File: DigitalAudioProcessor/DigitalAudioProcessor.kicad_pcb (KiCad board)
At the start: 4 copper layers, 40 x 40 mm, 65 parts, among them J1 SWD, J2 I2S_OUT, J3 I2S_1, J4 USB, J5 I2S_3, J6 I2C, J7 I2S_2, J8 3.3V, U1 TOSLINK_RX, U2 USBLC6-2SC6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

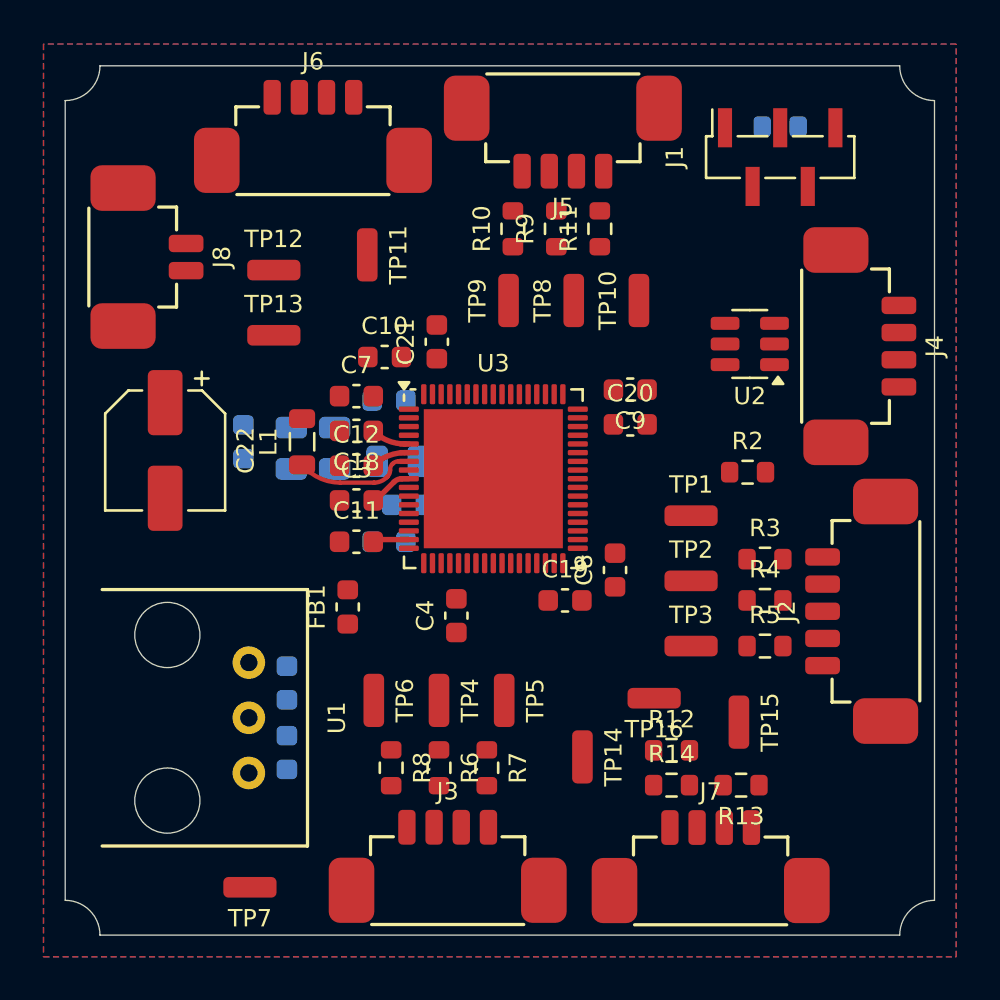
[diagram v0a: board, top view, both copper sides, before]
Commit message: DigitalAudioProcessor PCB done
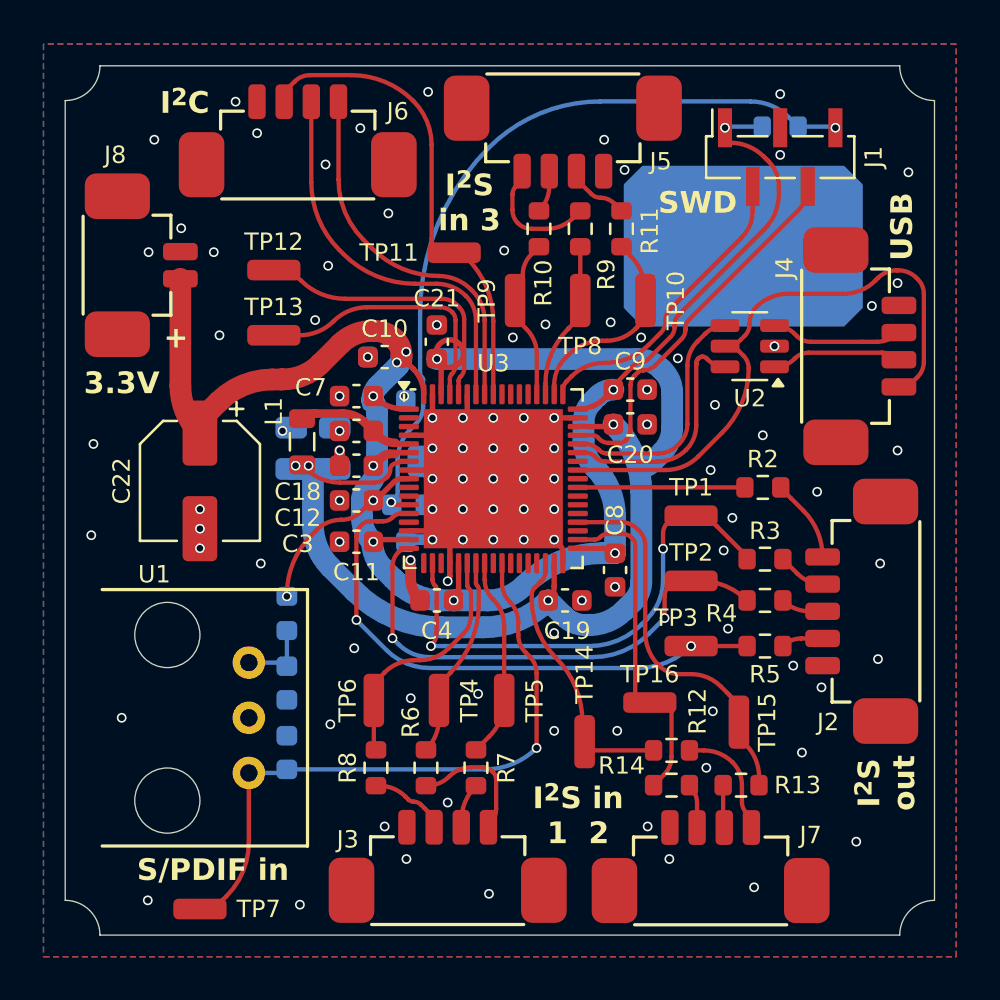
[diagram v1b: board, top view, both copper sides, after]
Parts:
- added REF**: BW_Logo_10x6.4mm, BW_Logo:BW_Logo_10x6.4mm, B.Cu at (161.2, 88.3)
- FB1: moved to B.Cu
- moved C2 7.58 mm to (144.7, 93.4), turned to 0 degrees
- moved TP11 4.00 mm to (147.9, 88.6), turned to 0 degrees
- moved FB1 2.82 mm to (140.2, 105.2), turned to -90 degrees
- moved TP7 2.51 mm to (136.2, 118.8)
- moved C22 2.13 mm to (136.2, 99.1)
- moved R10 1.20 mm to (151.8, 87.5)
- moved C4 1.14 mm to (147.1, 104.6), turned to 0 degrees
- moved R9 1.10 mm to (153.7, 87.5)
- moved R11 1.00 mm to (155.6, 87.5)
- moved R2 0.99 mm to (162.1, 99.4)
- moved J6 0.73 mm to (140.7, 84.1)
- moved TP14 0.71 mm to (153.9, 111.1)
- moved R8 0.70 mm to (144.3, 112.3)
- moved R6 0.60 mm to (146.6, 112.3)
- moved R7 0.50 mm to (148.9, 112.3)
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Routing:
- net +3.3V: track 5.46 -> 90.5 mm, vias 0 -> 11
- net VCC: track 5.66 -> 58.3 mm, vias 0 -> 5
- net Net-(J1-Pin_5): track 0.00 -> 35.4 mm, vias 0 -> 2
- net Net-(U1-OUT): track 0.00 -> 29.8 mm, vias 0 -> 1
- net Net-(J4-Pin_1): track 0.00 -> 28.3 mm
- net /I2S_OUT_LRCK: track 0.00 -> 25.8 mm, vias 0 -> 2
- net GND: track 0.00 -> 23.5 mm, vias 0 -> 106
- net Net-(U3-PA2): track 0.00 -> 23.4 mm, vias 0 -> 2
- net Net-(U3-PA0): track 0.00 -> 23.3 mm, vias 0 -> 2
- net Net-(J6-Pin_3): track 0.00 -> 22.1 mm
- net Net-(J6-Pin_2): track 0.00 -> 18.2 mm
- net /SWDIO: track 0.00 -> 17.5 mm
- net Net-(U3-PB14): track 0.00 -> 17.5 mm
- net Net-(J6-Pin_1): track 0.00 -> 17.2 mm
- net Net-(U3-PB12): track 0.00 -> 15.6 mm
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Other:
- board text added: "+"
- board text added: "3.3V"
- board text added: "I^{2}C"
- board text added: "I^{2}S in 1 2"
- board text added: "I^{2}S in 3"
- board text added: "I^{2}S out"
- board text added: "Modular Audio Digital Audio Processor"
- board text added: "S/PDIF in"
- board text added: "SWD"
- board text added: "USB"

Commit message: DigitalAudioProcessor net labels
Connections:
- net Net-(J4-Pin_1) renamed /USB_VBUS
- net Net-(J6-Pin_1) renamed /I2C_SCL
- net Net-(J6-Pin_2) renamed /I2C_SDA
- net Net-(J6-Pin_3) renamed /I2C_~{INT}
- net Net-(U1-OUT) renamed /SPDIF_IN
- net Net-(U3-PA0) renamed /I2S_OUT_DATA
- net Net-(U3-PA11) renamed /USB_D-
- net Net-(U3-PA12) renamed /USB_D+
- net Net-(U3-PA2) renamed /I2S_OUT_BCK
- net Net-(U3-PA4) renamed /I2S_1_LRCK
- net Net-(U3-PA5) renamed /I2S_1_BCK
- net Net-(U3-PA6) renamed /I2S_1_DATA
- net Net-(U3-PB10) renamed /I2S_2_BCK
- net Net-(U3-PB12) renamed /I2S_2_LRCK
- net Net-(U3-PB14) renamed /I2S_2_DATA
- net Net-(U3-PB8) renamed /DEBUG_RX
- net Net-(U3-PB9) renamed /DEBUG_TX
- net Net-(U3-PC10) renamed /I2S_3_BCK
- net Net-(U3-PC11) renamed /I2S_3_DATA

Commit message: DigitalAudioProcessor fixed USB disconnect detection
Pull-down on the USB_VBUS line is required to consistently detect disconnection.
Firmware adjusted to not flush buffer on disconnect, as that causes a long freeze - seems to work fine without it too.
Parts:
- added R15: 1kΩ, Resistor_SMD:R_0603_1608Metric, F.Cu at (161.0, 96.7)
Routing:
- net GND: track 23.5 -> 24.1 mm
